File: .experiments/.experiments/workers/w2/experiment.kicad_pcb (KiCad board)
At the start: 2 copper layers, 140 x 90 mm, 39 parts, among them J1 USB_C, J2 Output, J3 Debug, Q1 FS8205A, U1 USBLC6-2SC6, U2 BQ24072, U3 HY2113-KB5B, U4 MT3608, U5 AP2112K-3.3, U6 LN61CN3302MR-G

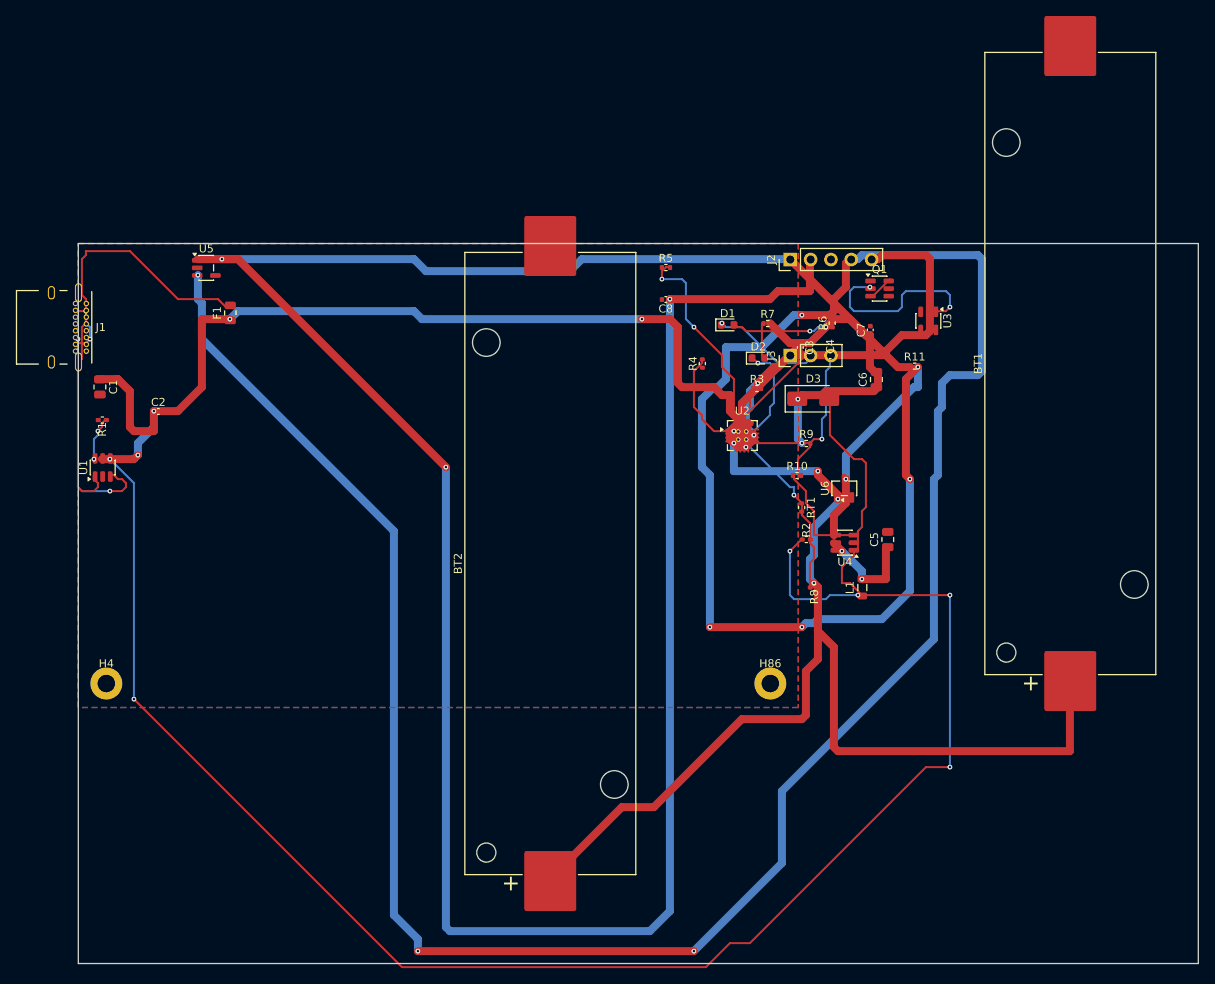
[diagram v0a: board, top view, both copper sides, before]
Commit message: Set uniform 6mil trace width (0.1524mm) for signal+power to reduce shorts
Baseline with 6mil: score=20.05 shorts=72 (vs 25.66@82shorts before)
Round 1: 20.45 shorts=93
Round 2: 20.65 shorts=84 [NEW BEST]
Round 3: 19.44 shorts=72

Trading off routing flexibility for cleaner DRC (no catastrophic shorts).
Tighter routing but more predictable.

Co-Authored-By: Claude Opus 4.6 <noreply@anthropic.com>
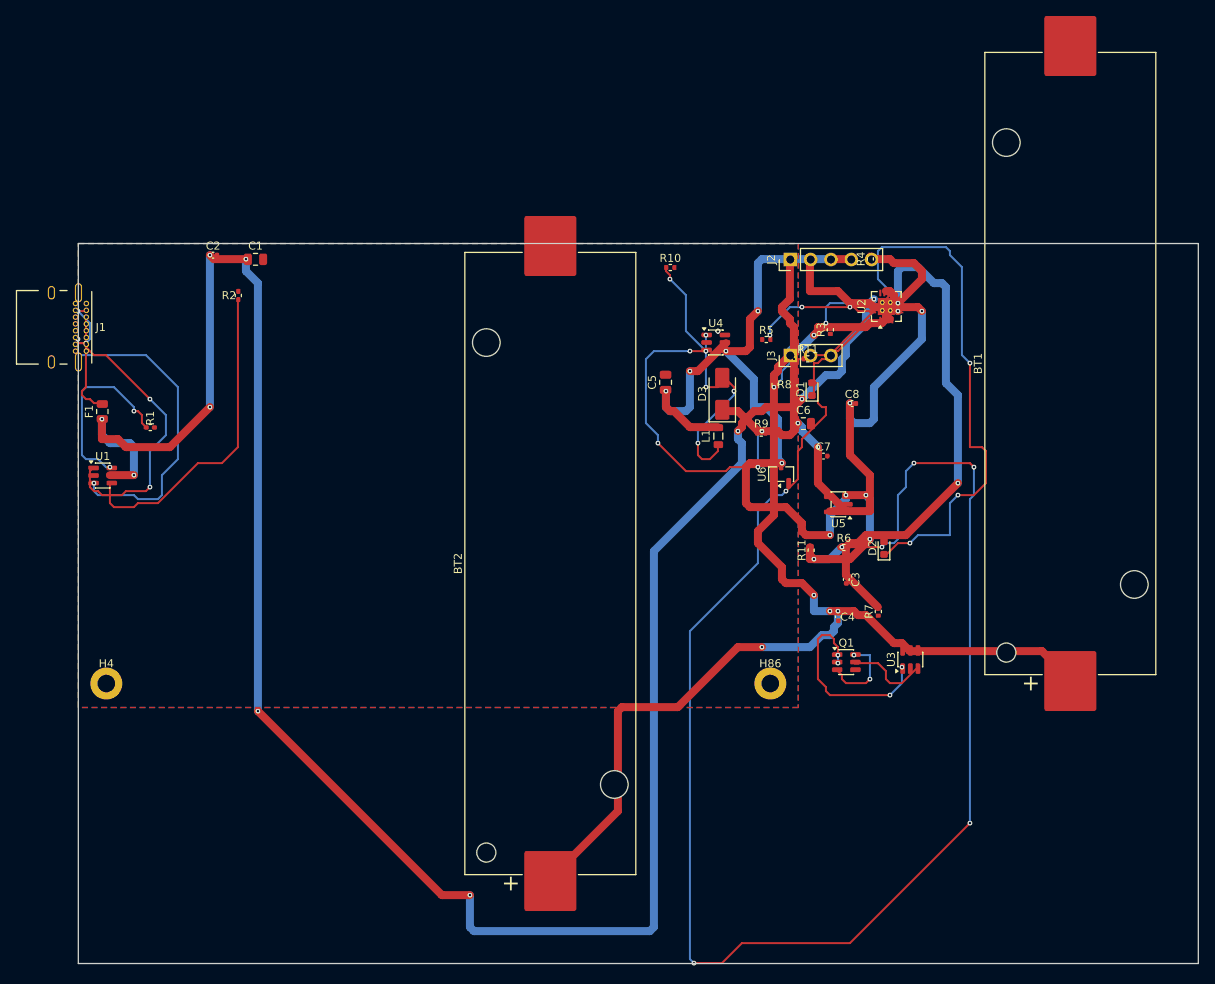
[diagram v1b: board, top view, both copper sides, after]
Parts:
- moved U5 84.3 mm to (95.0, 32.6), turned to 180 degrees
- moved R2 77.3 mm to (20.0, 6.50), turned to 90 degrees
- moved Q1 46.9 mm to (96.0, 52.3)
- moved U3 42.4 mm to (104.0, 52.0), turned to 90 degrees
- moved R7 38.6 mm to (100.0, 46.0), turned to 90 degrees
- moved C5 34.0 mm to (73.4, 17.3)
- moved C4 32.7 mm to (95.0, 46.7), turned to -90 degrees
- moved R10 30.4 mm to (74.0, 3.00)
- moved U4 29.8 mm to (79.7, 12.4), turned to 0 degrees
- moved C3 29.6 mm to (96.0, 42.0)
- moved D2 28.5 mm to (100.7, 38.1), turned to 90 degrees
- moved R6 28.1 mm to (95.7, 38.0), turned to 0 degrees
- moved C8 26.7 mm to (96.7, 20.0), turned to 0 degrees
- moved R11 26.4 mm to (91.6, 38.3), turned to 90 degrees
- moved L1 26.1 mm to (80.0, 24.1)
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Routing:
- net /EN: track 391.7 -> 89.6 mm, vias 10 -> 8
- net Net-(D1-A): track 13.1 -> 193.9 mm, vias 2 -> 6
- net Net-(R2-Pad1): track 207.0 -> 40.3 mm, vias 6 -> 0
- net /3V3: track 224.9 -> 60.0 mm
- net /VBUS: track 121.6 -> 269.7 mm, vias 4 -> 10
- net /5V: track 112.4 -> 47.0 mm, vias 4 -> 2
- net Net-(D2-K): track 14.4 -> 67.3 mm, vias 2 -> 4
- net /VBAT: track 198.0 -> 161.6 mm, vias 4 -> 6
- net Net-(U4-FB): track 18.4 -> 51.0 mm, vias 0 -> 6
- net /VSYS: track 40.3 -> 72.6 mm, vias 2 -> 6
- net /NTC_SENSE: track 38.6 -> 17.6 mm
- net /CHG_N: track 35.6 -> 17.7 mm, vias 4 -> 0
- net Net-(F1-Pad2): track 35.2 -> 17.4 mm
- net Net-(R1-Pad1): track 5.62 -> 23.3 mm
- net Net-(U2-ILIM): track 15.4 -> 0.00 mm
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
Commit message: Clean up: remove 50M+ of old experiment artifacts
Removed:
- .tmp_router_regression/ (11M baseline)
- .experiments/workers/ (40M+ old copies)
- .experiments/frames/ (old snapshots)

Kept: latest PCB, GIF, config, results

Co-Authored-By: Claude Opus 4.6 <noreply@anthropic.com>
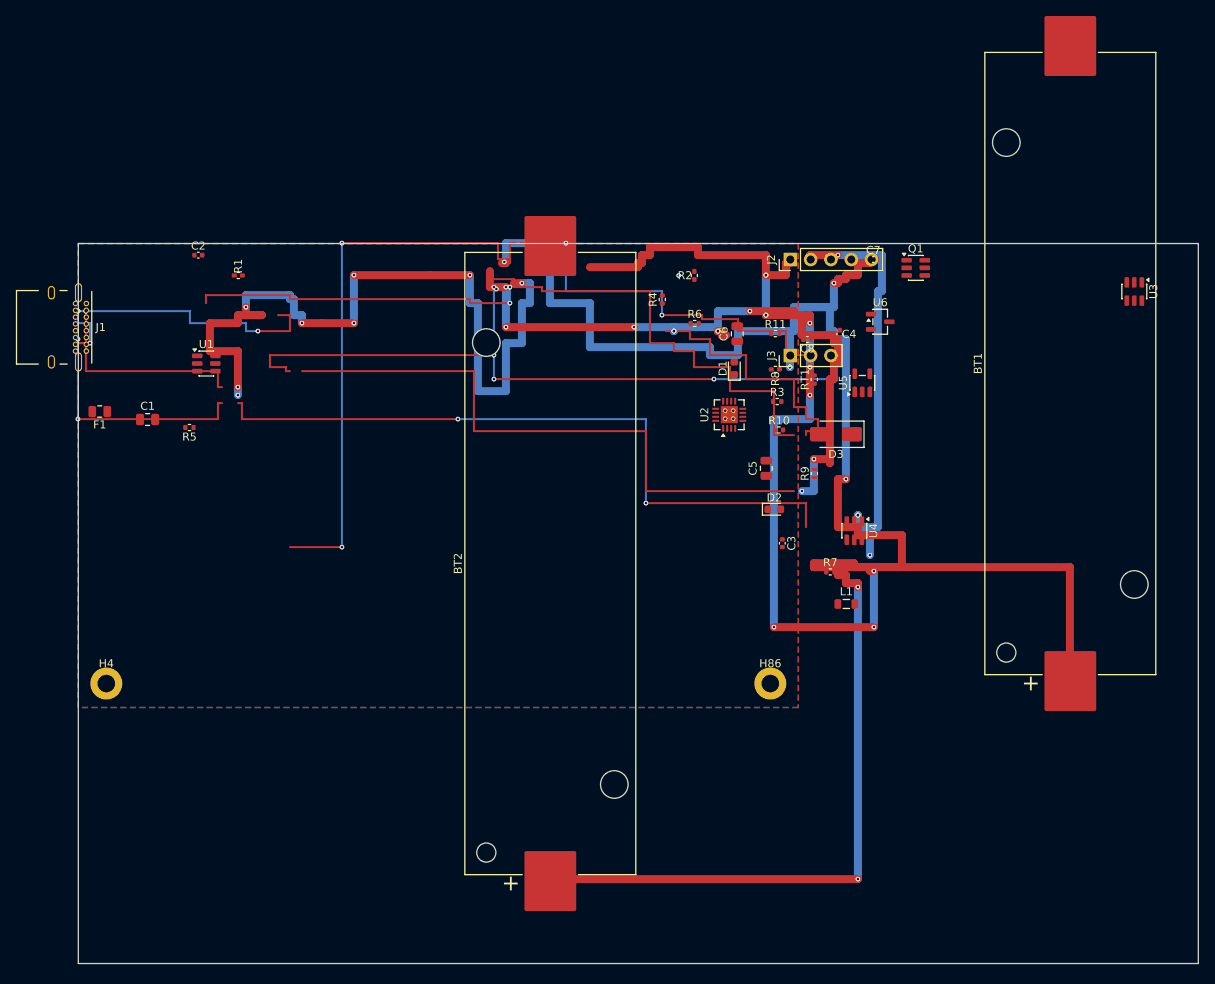
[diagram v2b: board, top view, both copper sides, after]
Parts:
- moved R5 72.9 mm to (13.9, 23.0), turned to 180 degrees
- moved R2 57.1 mm to (77.0, 4.00)
- moved U3 53.9 mm to (132.0, 6.00), turned to -90 degrees
- moved Q1 50.0 mm to (104.7, 3.04)
- moved C4 35.4 mm to (95.2, 11.3)
- moved R6 33.6 mm to (77.0, 10.0)
- moved U4 29.2 mm to (97.0, 35.9), turned to -90 degrees
- moved R11 27.4 mm to (87.1, 11.3), turned to 0 degrees
- moved R4 26.5 mm to (73.0, 7.00)
- moved L1 26.4 mm to (96.0, 45.1), turned to 0 degrees
- moved C7 25.3 mm to (99.4, 2.00)
- moved R10 24.4 mm to (87.6, 23.3)
- moved C1 24.1 mm to (8.66, 22.0)
- moved U2 23.9 mm to (81.4, 21.4)
- moved U6 22.7 mm to (100.2, 9.78), turned to 0 degrees
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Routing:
- net /VBUS: track 269.7 -> 99.5 mm, vias 10 -> 8
- net /VBAT: track 161.6 -> 279.5 mm, vias 6 -> 10
- net Net-(D1-A): track 193.9 -> 76.5 mm, vias 6 -> 0
- net /NTC_SENSE: track 17.6 -> 123.0 mm, vias 2 -> 4
- net /EN: track 89.6 -> 0.00 mm, vias 8 -> 0
- net /CHG_N: track 17.7 -> 99.5 mm, vias 0 -> 6
- net /5V: track 47.0 -> 112.0 mm, vias 2 -> 11
- net Net-(U4-FB): track 51.0 -> 0.00 mm, vias 6 -> 0
- net Net-(R2-Pad1): track 40.3 -> 86.5 mm, vias 0 -> 2
- net Net-(U2-ILIM): track 0.00 -> 42.0 mm, vias 0 -> 2
- net Net-(D2-A): track 0.00 -> 33.5 mm
- net Net-(D3-A): track 25.6 -> 0.00 mm, vias 4 -> 0
- net /VSYS_BOOST: track 25.4 -> 0.00 mm, vias 2 -> 0
- net Net-(Q1A-G): track 24.9 -> 0.00 mm, vias 4 -> 0
- net Net-(R1-Pad1): track 23.3 -> 0.00 mm, vias 2 -> 0
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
